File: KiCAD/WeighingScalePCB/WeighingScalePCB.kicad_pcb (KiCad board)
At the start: 2 copper layers, 94.6 x 51.1 mm, 47 parts, among them IC1 MAX6675ISA+T, IC2 APS11753KMDALX-9PL5, IC3 CAP1203-1-SN, J1 Conn_01x14_MountingPin, J2 AudioJack4, J4 Battery Conn, J6 Conn_01x04_MountingPin, Q5 NX138AKR, T1 TouchPad, T2 TouchPad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

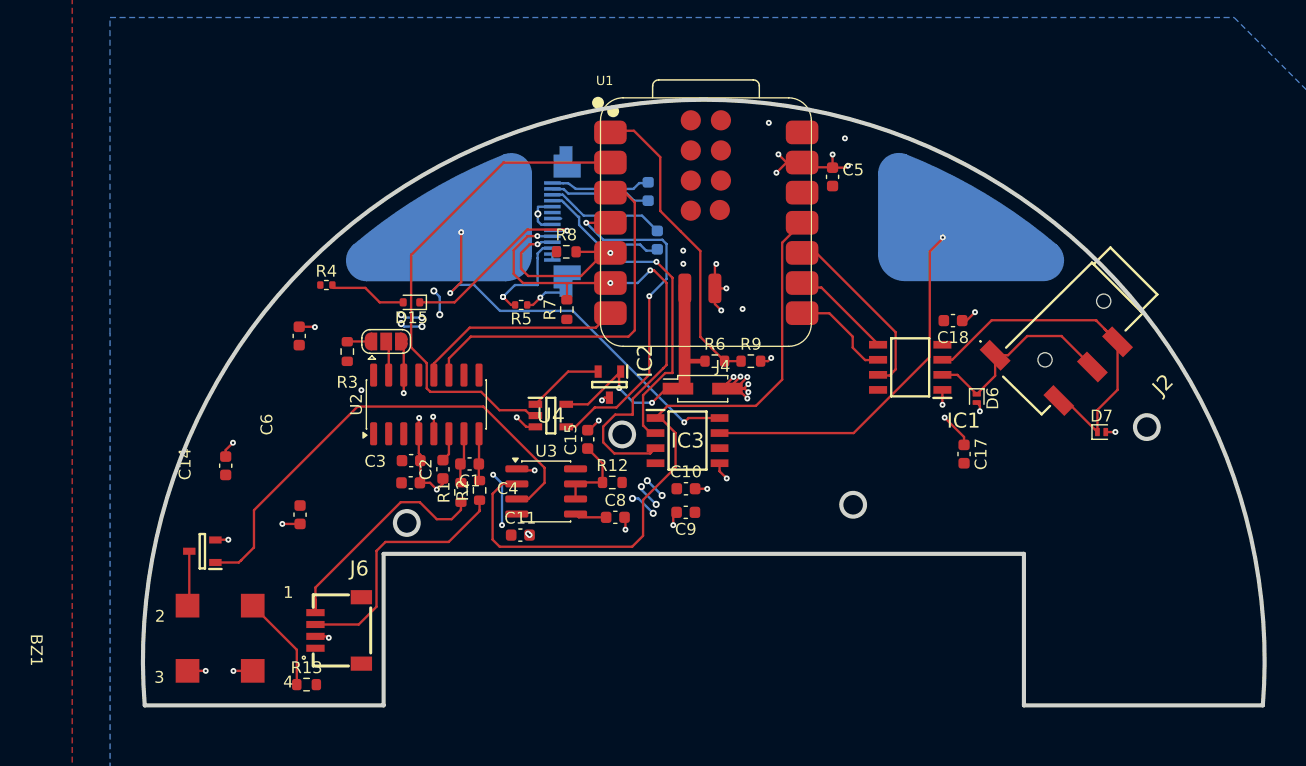
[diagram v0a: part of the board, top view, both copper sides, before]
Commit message: version added, artwork added, gerber updated accordingly
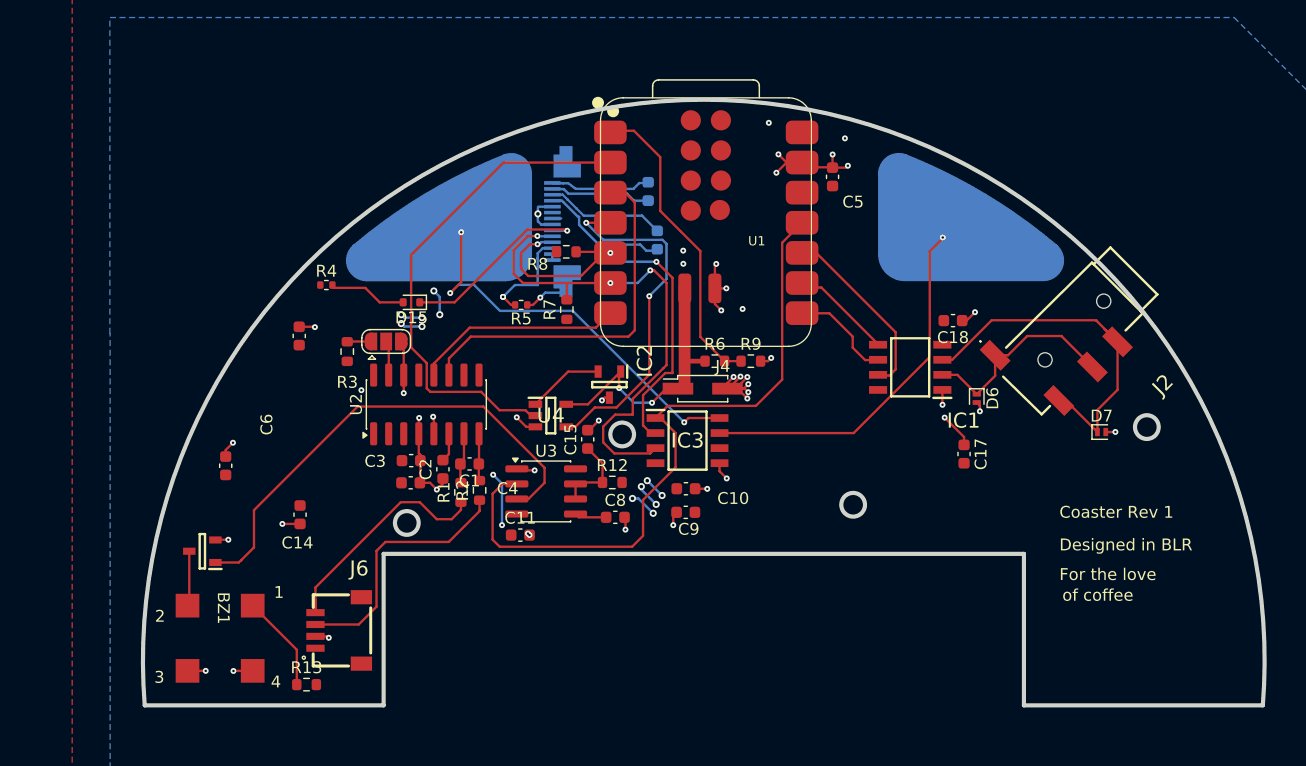
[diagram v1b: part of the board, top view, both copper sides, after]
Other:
- board text added: "Coaster Rev 1"
- board text added: "Designed in BLR"
- board text added: "For the love"
- board text added: "of coffee"
